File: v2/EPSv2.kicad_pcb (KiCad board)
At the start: 4 copper layers, 50 x 110 mm, 168 parts, among them J1 Conn_01x03, J10 Conn_01x05_Pin, J2 Conn_01x03, J3 Conn_01x02, J4 5037630491, J5 2P 21700 Cell Holder, J6 5037630491, J7 1053091102, J8 1053091102, J9 1053091102, Q1 AO3400A, Q2 AO3400A, Q3 AO3400A, Q4 AO3400A, Q5 AP25P06K, Q6 AP25P06K, Q7 AP25P06K, U1 BQ29700DSER, U10 TPS63070RNMR, U11 LM73100RPWR, U12 LM73100RPWR, U13 TPS63070RNMR, U14 ISO1044BD, U2 BQ29700DSER, U3 MCP73831T-2ACI/OT, U4 MCP73831T-2ACI/OT, U5 LM73100RPWR, U6 C3235556 (M66200DRLR), U7 C3235556 (M66200DRLR), U8 STM32L432KCUx, U9 TPS63070RNMR

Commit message: cleared unrouted
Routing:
- net Net-(J4-CANL): track 36.3 -> 33.7 mm
- net /STM32L432KCUx/SWDIO: track 57.4 -> 56.8 mm
- net /BQ29700_2/CELL+: vias 12 -> 18

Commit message: minor changes for silkscreen
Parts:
- moved G*** 0.38 mm to (-20.8, -14.7)
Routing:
- net /STM32L432KCUx/I2C1_SDA: track 1.85 -> 0.00 mm, vias 1 -> 0
- net TEMP_2: track 77.6 -> 79.1 mm
- net /STM32L432KCUx/I2C1_SCL: track 1.18 -> 0.00 mm, vias 1 -> 0
- net CAN_TX: vias 3 -> 2
- net CAN_RX: vias 3 -> 2
- added copper zone on F.Cu, net (none)
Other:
- board text added: "CELL_1+"
- board text added: "CELL_2+"
- board text added: "JP4/5/6 = Load Switch Bypass"
- board text added: "TEMP_1"
- board text added: "TEMP_2"

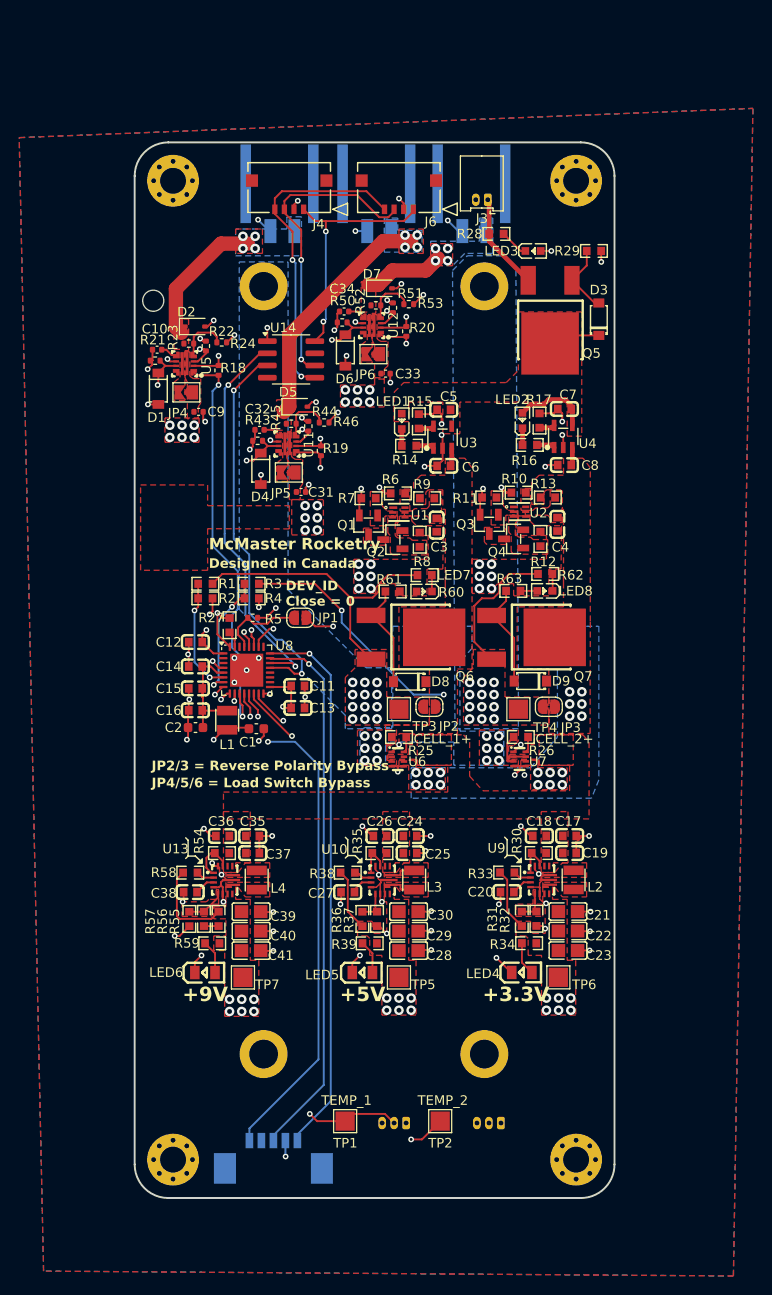
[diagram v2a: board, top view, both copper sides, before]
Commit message: bigger current ratings for 5V and 9V
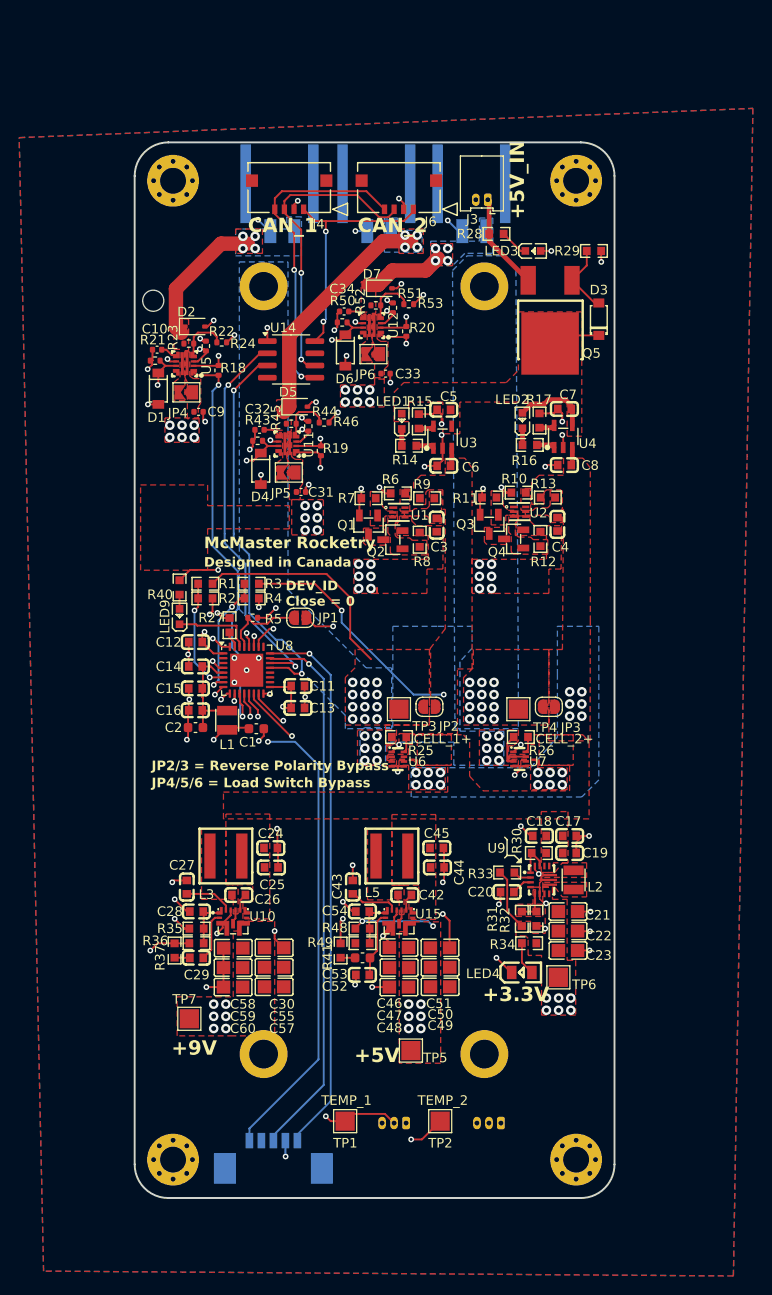
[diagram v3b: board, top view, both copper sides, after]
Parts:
- removed C35, C36, C37: 10uF 0603, Rocketry_Easyeda:C0603
- removed C38: 100nF 0603, Rocketry_Easyeda:C0603
- removed C39, C40, C41: 22uF 0805, Rocketry_Easyeda:C0805
- removed D8, D9: BZT52C11-7-F, Rocketry_Easyeda:SOD-123_L2.8-W1.8-LS3.7-RD
- removed L4: 1.5uF 2.9A, Rocketry_Easyeda:IND-SMD_L2.5-W2.0_MEKK2520TR47M
- removed LED5, LED6: 0805G (Green), Rocketry_Easyeda:LED0805-R-RD
- removed LED7, LED8: KT-0603R (RED), Rocketry_Easyeda:LED0603-RD
- removed Q6, Q7: AP25P06K, Rocketry_Easyeda:TO-252-2_L6.6-W6.1-P4.57-LS10.1-BL
- removed R38, R58: 100k 0603, Rocketry_Easyeda:R0603
- removed R39: 2.2k 0603, Rocketry_Easyeda:R0603
- removed R54: 10k 0603, Rocketry_Easyeda:R0603
- removed R55: 300k 0603, Rocketry_Easyeda:R0603
- removed R56, R57: 33k 0603, Rocketry_Easyeda:R0603
- removed R59: 0603WAF5101T5E (5.1k 0603), Rocketry_Easyeda:R0603
- removed R60, R62: 0603WAF1001T5E (1k 0603), Rocketry_Easyeda:R0603
- removed R61, R63: 0603WAF1003T5E (100k 0603), Rocketry_Easyeda:R0603
- removed U13: TPS63070RNMR, Rocketry_Easyeda:VQFN-HR-15_L3.0-W2.5-P0.50-BL_TPS63070RNMR
- added C42: CC0603KRX7R9BB104 (100nF 0603), Rocketry_Easyeda:C0603, F.Cu at (3.14, 23.4)
- added C43: CL10A225KO8NNNC, Rocketry_Easyeda:C0603, F.Cu at (-2.27, 22.6)
- added C44: CC0603KRX7R9BB104 (100nF 0603), Rocketry_Easyeda:C0603, F.Cu at (6.54, 20.6)
- added C45: CL10A106KP8NNNC (10uF 0603), Rocketry_Easyeda:C0603, F.Cu at (6.48, 18.5)
- added C46: CL21A226MAQNNNE (22uF 0805), Rocketry_Easyeda:C0805, F.Cu at (2.54, 28.9)
- added C47: CL21A226MAQNNNE (22uF 0805), Rocketry_Easyeda:C0805, F.Cu at (2.56, 31.0)
- added C48: CL21A226MAQNNNE (22uF 0805), Rocketry_Easyeda:C0805, F.Cu at (2.54, 33.0)
- added C49: CL21A226MAQNNNE (22uF 0805), Rocketry_Easyeda:C0805, F.Cu at (6.83, 33.0)
- added C50: CL21A226MAQNNNE (22uF 0805), Rocketry_Easyeda:C0805, F.Cu at (6.83, 31.0)
- added C51: CL21A226MAQNNNE (22uF 0805), Rocketry_Easyeda:C0805, F.Cu at (6.81, 28.9)
- added C52: CL10C220JB8NNNC, Rocketry_Easyeda:C0603, F.Cu at (-1.25, 31.8)
- added C53: 33nF, Capacitor_SMD:C_0603_1608Metric, F.Cu at (-1.25, 30.0)
- added C54: CL10C270JB8NNNC, Rocketry_Easyeda:C0603, F.Cu at (-1.25, 25.1)
- added C55: CL21A226MAQNNNE (22uF 0805), Rocketry_Easyeda:C0805, F.Cu at (-10.5, 31.0)
- added C57: CL21A226MAQNNNE (22uF 0805), Rocketry_Easyeda:C0805, F.Cu at (-10.5, 33.0)
- added C58: CL21A226MAQNNNE (22uF 0805), Rocketry_Easyeda:C0805, F.Cu at (-14.7, 29.0)
- added C59: CL21A226MAQNNNE (22uF 0805), Rocketry_Easyeda:C0805, F.Cu at (-14.7, 31.0)
- added C60: CL21A226MAQNNNE (22uF 0805), Rocketry_Easyeda:C0805, F.Cu at (-14.7, 33.0)
- added L5: SRP5030CA-2R2M, Rocketry_Easyeda:IND-SMD_L5.5-W5.3, F.Cu at (1.81, 19.4)
- added LED9: Yellow, Rocketry_Easyeda:LED0603-RD-YELLOW, F.Cu at (-20.3, -5.59)
- added R40: 0603WAF1001T5E (1k 0603), Rocketry_Easyeda:R0603, F.Cu at (-20.3, -8.62)
- added R41: FRC0603F5761TS, Rocketry_Easyeda:R0603, F.Cu at (-3.54, 29.2)
- added R48: 0603WAF1372T5E, Rocketry_Easyeda:R0603, F.Cu at (-1.25, 26.9)
- added R49: 0603WAF1003T5E (100k 0603), Rocketry_Easyeda:R0603, F.Cu at (-1.25, 28.4)
- added U15: TPS61288LRQQR, Rocketry_Easyeda:VQFN-HR-11_L3.0-W2.5-P0.50-TL, F.Cu at (2.56, 25.7)
- C24: value 10uF 0603 -> CL10A106KP8NNNC (10uF 0603)
- C25, C26: value 10uF 0603 -> CC0603KRX7R9BB104 (100nF 0603)
- C27: value 100nF 0603 -> CL10A225KO8NNNC
- C28: value 22uF 0805 -> CL10C270JB8NNNC; footprint Rocketry_Easyeda:C0805 -> Rocketry_Easyeda:C0603
- C29: value 22uF 0805 -> CC0603KRX7R9BB203; footprint Rocketry_Easyeda:C0805 -> Rocketry_Easyeda:C0603
- C30: value 22uF 0805 -> CL21A226MAQNNNE (22uF 0805)
- L3: value 1.5uF 2.9A -> SRP5030CA-2R2M; footprint Rocketry_Easyeda:IND-SMD_L2.5-W2.0_MEKK2520TR47M -> Rocketry_Easyeda:IND-SMD_L5.5-W5.3
- R35: value 10k 0603 -> FRC0603F1432TS
- R36: value 680k 0603 -> 0603WAF2003T5E
- R37: value 130k 0603 -> FRC0603F1872TS
- U10: value TPS63070RNMR -> TPS61288LRQQR; footprint Rocketry_Easyeda:VQFN-HR-15_L3.0-W2.5-P0.50-BL_TPS63070RNMR -> Rocketry_Easyeda:VQFN-HR-11_L3.0-W2.5-P0.50-TL
- moved C28 22.5 mm to (-18.6, 25.1), turned to 0 degrees
- moved C29 22.3 mm to (-18.6, 30.0), turned to 0 degrees
- moved R37 21.4 mm to (-20.8, 29.2), turned to -90 degrees
- moved R35 20.6 mm to (-18.6, 26.9), turned to 180 degrees
- moved L3 19.8 mm to (-15.5, 19.4), turned to 180 degrees
- moved R36 17.5 mm to (-18.6, 28.4), turned to 0 degrees
- moved C27 16.8 mm to (-19.6, 22.6), turned to -90 degrees
- moved C26 16.0 mm to (-14.2, 23.4), turned to 180 degrees
- moved U10 15.9 mm to (-14.7, 25.7), turned to 0 degrees
- moved C24 14.6 mm to (-10.8, 18.5)
- moved C25 14.5 mm to (-10.8, 20.6)
- moved C30 14.5 mm to (-10.5, 28.9)
- moved TP5 7.72 mm to (3.79, 39.6)
- moved TP7 7.05 mm to (-19.3, 36.3)
- moved G*** 0.57 mm to (-21.1, -14.2)
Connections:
- C26 pad 1: GND -> Net-(U10-BST)
- C26 pad 2: /LM66200_2/VOUT -> Net-(C26-Pad2)
- C27 pad 2: Net-(U10-Vaux) -> Net-(U10-VCC)
- C28 pad 2: +5V -> Net-(U10-FB)
- C29 pad 1: GND -> Net-(C29-Pad1)
- C29 pad 2: +5V -> Net-(U10-COMP)
- C30 pad 2: +5V -> +9V
- C6 pad 2: /BQ29700_1/CELL+ -> CELL_1+
- C8 pad 2: /BQ29700_2/CELL+ -> CELL_2+
- JP2 pad 1: /BQ29700_1/CELL+ -> CELL_1+
- JP3 pad 1: /BQ29700_2/CELL+ -> CELL_2+
- L3 pad 1: Net-(U10-L1) -> /LM66200_2/VOUT
- L3 pad 2: Net-(U10-L2) -> Net-(C26-Pad2)
- R13 pad 2: /BQ29700_2/CELL+ -> CELL_2+
- R25 pad 2: /BQ29700_1/CELL+ -> CELL_1+
- R26 pad 2: /BQ29700_1/CELL+ -> CELL_1+
- R35 pad 1: Net-(U10-EN) -> Net-(U10-FB)
- R35 pad 2: /LM66200_2/VOUT -> +9V
- R36 pad 1: Net-(U10-FB) -> GND
- R36 pad 2: +5V -> Net-(U10-FB)
- R37 pad 2: Net-(U10-FB) -> Net-(C29-Pad1)
- R9 pad 2: /BQ29700_1/CELL+ -> CELL_1+
- U10 pad 1: Net-(U10-EN) -> Net-(U10-FB)
- U10 pad 11: Net-(U10-L1) -> Net-(U10-VCC)
- U10 pad 2: Net-(U10-PG) -> Net-(U10-COMP)
- U10 pad 3: Net-(U10-Vaux) -> GND
- U10 pad 4: GND -> Net-(C26-Pad2)
- U10 pad 5: Net-(U10-FB) -> +9V
- U10 pad 6: GND -> /LM66200_2/VOUT
- U10 pad 7: +5V -> /LM66200_2/VOUT
- U10 pad 8: +5V -> Net-(U10-BST)
- U10 pad 9: Net-(U10-L2) -> Net-(C26-Pad2)
- U3 pad 3: /BQ29700_1/CELL+ -> CELL_1+
- U4 pad 3: /BQ29700_2/CELL+ -> CELL_2+
- U6 pad 3: /BQ29700_1/CELL+ -> CELL_1+
- U6 pad 6: /BQ29700_2/CELL+ -> CELL_2+
- U7 pad 3: /BQ29700_1/CELL+ -> CELL_1+
- U7 pad 6: /BQ29700_2/CELL+ -> CELL_2+
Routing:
- net CELL_2+: track 42.3 -> 29.4 mm, vias 14 -> 32
- net Net-(D9-A): track 11.0 -> 0.00 mm
- net Net-(D8-A): track 11.0 -> 0.00 mm
- net /STM32L432KCUx/PB7: track 0.00 -> 8.33 mm
- net +9V: track 9.57 -> 1.94 mm, vias 12 -> 13
- net Net-(U15-COMP): track 0.00 -> 6.93 mm
- net /BQ29700_1/CELL+: track 5.30 -> 0.00 mm, vias 12 -> 0
- net Net-(U15-FB): track 0.00 -> 5.23 mm
- net Net-(U10-COMP): track 0.00 -> 5.15 mm
- net Net-(U15-VCC): track 0.00 -> 5.05 mm
- net Net-(U10-VCC): track 0.00 -> 5.05 mm
- net Net-(U13-EN): track 4.78 -> 0.00 mm
- net +3.3V: track 26.7 -> 30.9 mm, vias 20 -> 21
- net Net-(U13-FB): track 3.98 -> 0.00 mm
- net Net-(U10-EN): track 3.80 -> 0.00 mm
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- added copper zone on F.Cu, net Net-(C26-Pad2)
- added copper zone on F.Cu, net Net-(C42-Pad2)
- removed copper zone on B.Cu, net /BQ29700_1/CELL+
- removed copper zone on F.Cu, net /BQ29700_1/CELL+
- removed copper zone on B.Cu, net /BQ29700_2/CELL+
- removed copper zone on F.Cu, net /BQ29700_2/CELL+
- removed copper zone on F.Cu, net Net-(U13-FB)
- removed copper zone on F.Cu, net Net-(U13-L1)
- removed copper zone on F.Cu, net Net-(U13-L2)
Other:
- board text added: "+5V_IN"
- board text added: "CAN_1"
- board text added: "CAN_2"
- board text added: "EPS v2.1"
- board text added: "SWCLK +3.3V SWDIO GND nRST"
- board text removed: "EPS v2"
